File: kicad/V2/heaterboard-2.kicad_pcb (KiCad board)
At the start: 2 copper layers, 12 parts, among them J1 Screw_Terminal_01x02, J2 Conn_01x05_Pin, J3 Conn_01x04_Pin, Q1 Q_NMOS_GDS, U1 LM317_TO-220

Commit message: pcb updates
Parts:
- moved J1 114.5 mm to (50.8, 101.6), turned to 90 degrees
- moved U1 113.6 mm to (50.8, 88.9)
- moved R5 84.2 mm to (48.3, 71.1)
- moved R6 84.2 mm to (48.3, 78.7)
- moved Q1 82.9 mm to (81.3, 78.7)
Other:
- copper layers 2 -> 4
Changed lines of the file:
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@@
   (layers
     (0 "F.Cu" signal)
+    (1 "In1.Cu" signal)
+    (2 "In2.Cu" signal)
     (31 "B.Cu" signal)
     (32 "B.Adhes" user "B.Adhesive")
@@
   )
   (setup
+    (stackup
+      (layer "F.SilkS" (type "Top Silk Screen"))
+      (layer "F.Paste" (type "Top Solder Paste"))
+      (layer "F.Mask" (type "Top Solder Mask") (thickness 0.01))
+      (layer "F.Cu" (type "copper") (thickness 0.035))
+      (layer "dielectric 1" (type "prepreg") (thickness 0.1) (material "FR4") (epsilon_r 4.5) (loss_tangent 0.02))
+      (layer "In1.Cu" (type "copper") (thickness 0.035))
+      (layer "dielectric 2" (type "core") (thickness 1.24) (material "FR4") (epsilon_r 4.5) (loss_tangent 0.02))
+      (layer "In2.Cu" (type "copper") (thickness 0.035))
+      (layer "dielectric 3" (type "prepreg") (thickness 0.1) (material "FR4") (epsilon_r 4.5) (loss_tangent 0.02))
+      (layer "B.Cu" (type "copper") (thickness 0.035))
+      (layer "B.Mask" (type "Bottom Solder Mask") (thickness 0.01))
+      (layer "B.Paste" (type "Bottom Solder Paste"))
+      (layer "B.SilkS" (type "Bottom Silk Screen"))
+      (copper_finish "None")
+      (dielectric_constraints no)
+    )
     (pad_to_mask_clearance 0)
     (pcbplotparams
@@
   (net 37 "Net-(R5--)")
   (footprint "Package_TO_SOT_THT:TO-220-3_Vertical" (layer "F.Cu")
-    (at 162.56 62.62)
+    (at 81.28 78.74)
     (descr "TO-220-3, Vertical, RM 2.54mm, see https://www.vishay.com/docs/66542/to-220-1.pdf")
     (tags "TO-220-3 Vertical RM 2.54mm")
@@
   )
   (footprint "Resistor_THT:R_Axial_DIN0207_L6.3mm_D2.5mm_P10.16mm_Horizontal" (layer "F.Cu")
-    (at 132.08 86.36)
+    (at 48.26 78.74)
     (descr "Resistor, Axial_DIN0207 series, Axial, Horizontal, pin pitch=10.16mm, 0.25W = 1/4W, length*diameter=6.3*2.5mm^2, http://cdn-reichelt.de/documents/datenblatt/B400/1_4W%23YAG.pdf")
     (tags "Resistor Axial_DIN0207 series Axial Horizontal pin pitch 10.16mm 0.25W = 1/4W length 6.3mm diameter 2.5mm")
@@
   )
   (footprint "Package_TO_SOT_THT:TO-220-3_Vertical" (layer "F.Cu")
-    (at 162.56 68.58)
+    (at 50.8 88.9)
     (descr "TO-220-3, Vertical, RM 2.54mm, see https://www.vishay.com/docs/66542/to-220-1.pdf")
     (tags "TO-220-3 Vertical RM 2.54mm")
@@
   )
   (footprint "Resistor_THT:R_Axial_DIN0207_L6.3mm_D2.5mm_P10.16mm_Horizontal" (layer "F.Cu")
-    (at 132.08 78.74)
+    (at 48.26 71.12)
     (descr "Resistor, Axial_DIN0207 series, Axial, Horizontal, pin pitch=10.16mm, 0.25W = 1/4W, length*diameter=6.3*2.5mm^2, http://cdn-reichelt.de/documents/datenblatt/B400/1_4W%23YAG.pdf")
     (tags "Resistor Axial_DIN0207 series Axial Horizontal pin pitch 10.16mm 0.25W = 1/4W length 6.3mm diameter 2.5mm")
@@
   )
   (footprint "Connector_PinHeader_2.54mm:PinHeader_1x02_P2.54mm_Vertical" (layer "F.Cu")
-    (at 161.65 72.94)
+    (at 50.8 101.6 90)
     (descr "Through hole straight pin header, 1x02, 2.54mm pitch, single row")
     (tags "Through hole pin header THT 1x02 2.54mm single row")
@@
     (property "ki_keywords" "screw terminal")
     (attr through_hole)
-    (fp_text reference "J1" (at 0 -2.33) (layer "F.SilkS")
-        (effects (font (size 1 1) (thickness 0.15)))
-    )
-    (fp_text value "Screw_Terminal_01x02" (at 0 4.87) (layer "F.SilkS")
-        (effects (font (size 1 1) (thickness 0.15)))
-    )
-    (fp_text user "${REFERENCE}" (at 0 1.27 90) (layer "F.Fab")
+    (fp_text reference "J1" (at 0 -2.33 90) (layer "F.SilkS")
+        (effects (font (size 1 1) (thickness 0.15)))
+    )
+    (fp_text value "Screw_Terminal_01x02" (at 0 4.87 90) (layer "F.SilkS")
+        (effects (font (size 1 1) (thickness 0.15)))
+    )
+    (fp_text user "${REFERENCE}" (at 0 1.27) (layer "F.Fab")
         (effects (font (size 1 1) (thickness 0.15)))
     )
@@
     (fp_line (start 1.27 3.81) (end -1.27 3.81)
       (stroke (width 0.1) (type solid)) (layer "F.Fab"))
-    (pad "1" thru_hole rect (at 0 0) (size 1.7 1.7) (drill 1) (layers "*.Cu" "*.Mask")
+    (pad "1" thru_hole rect (at 0 0 90) (size 1.7 1.7) (drill 1) (layers "*.Cu" "*.Mask")
       (net 31 "Net-(J1-Pin_1)") (pinfunction "Pin_1") (pintype "passive"))
-    (pad "2" thru_hole oval (at 0 2.54) (size 1.7 1.7) (drill 1) (layers "*.Cu" "*.Mask")
+    (pad "2" thru_hole oval (at 0 2.54 90) (size 1.7 1.7) (drill 1) (layers "*.Cu" "*.Mask")
       (net 32 "+12V") (pinfunction "Pin_2") (pintype "passive"))
     (model "${KICAD6_3DMODEL_DIR}/Connector_PinHeader_2.54mm.3dshapes/PinHeader_1x02_P2.54mm_Vertical.wrl"

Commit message: pcb layout
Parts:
- added C1: 100nF, Capacitor_THT:CP_Radial_D10.0mm_P5.00mm, F.Cu at (127.0, 61.0)
- added C2: 1μF, Capacitor_THT:CP_Radial_D10.0mm_P5.00mm, F.Cu at (142.3, 61.0)
- J1: footprint Connector_PinHeader_2.54mm:PinHeader_1x02_P2.54mm_Vertical -> TerminalBlock:TerminalBlock_Wuerth_691311400102_P7.62mm
- R5: value 0.4 kΩ -> 0.4kΩ
- R6: value 2.4 kΩ -> 2.4kΩ
- moved R6 97.2 mm to (139.7, 45.7)
- moved J1 94.5 mm to (143.5, 83.4), turned to 180 degrees
- moved J2 88.7 mm to (66.0, 81.3), turned to 90 degrees
- moved R5 80.3 mm to (124.5, 45.7)
- moved J3 76.0 mm to (83.8, 81.3), turned to 90 degrees
- moved R1 68.6 mm to (63.5, 45.7)
- moved R2 54.3 mm to (78.7, 45.7)
- moved R3 42.0 mm to (94.0, 45.7)
- moved R4 34.2 mm to (109.2, 45.7)
- moved U1 31.8 mm to (66.0, 61.0)
- moved Q1 17.8 mm to (81.3, 61.0)
- moved A1 7.05 mm to (109.2, 97.8)
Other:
- board outline added: 113.2 x 68.2 mm

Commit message: pcb layout and began routing
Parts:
- added J1: Screw_Terminal_01x02, Connector_Molex:Molex_Mega-Fit_76825-0002_2x01_P5.70mm_Horizontal, F.Cu at (86.4, 87.2)
- J2: renamed from J1; footprint TerminalBlock:TerminalBlock_Wuerth_691311400102_P7.62mm -> Connector_Molex:Molex_Mega-Fit_76825-0002_2x01_P5.70mm_Horizontal
- J3: footprint Connector_PinSocket_2.54mm:PinSocket_1x04_P2.54mm_Vertical -> Connector_Molex:Molex_Micro-Fit_3.0_43650-0400_1x04_P3.00mm_Horizontal
- J4: renamed from J2; footprint Connector_PinHeader_2.54mm:PinHeader_1x05_P2.54mm_Vertical -> Connector_Molex:Molex_Micro-Fit_3.0_43650-0515_1x05_P3.00mm_Vertical
- moved J4 90.7 mm to (154.5, 61.0), turned to 0 degrees
- moved J3 84.1 mm to (166.9, 94.7), turned to 180 degrees
- moved R5 69.4 mm to (157.5, 73.7)
- moved R3 65.3 mm to (127.0, 61.0)
- moved R6 61.5 mm to (157.5, 83.8)
- moved R4 54.5 mm to (127.0, 71.1)
- moved R2 50.1 mm to (96.5, 71.1)
- moved Q1 42.0 mm to (99.1, 99.1)
- moved C1 40.8 mm to (86.4, 64.1), turned to -90 degrees
- moved U1 39.1 mm to (99.1, 81.8)
- moved A1 36.6 mm to (139.7, 118.1)
- moved R1 32.1 mm to (96.5, 61.5)
- moved J2 26.9 mm to (116.8, 86.8)
- moved C2 25.7 mm to (116.8, 64.1), turned to -90 degrees
- renumbered R5 to R1, R6 to R2, R1 to R3, R2 to R4, R3 to R5, R4 to R6
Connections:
- R4 pad 2: unconnected-(R2---Pad2) -> GND
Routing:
- net +9V: track 0.00 -> 98.1 mm
- net /A0: track 0.00 -> 17.3 mm
- net /A1: track 0.00 -> 17.3 mm
- net Net-(R1--): track 0.00 -> 16.8 mm
- net GND: track 0.00 -> 11.0 mm
- added copper zone on In1.Cu, net (none)
- added copper zone on In2.Cu, net (none)
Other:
- outline, holes or cut-outs redrawn

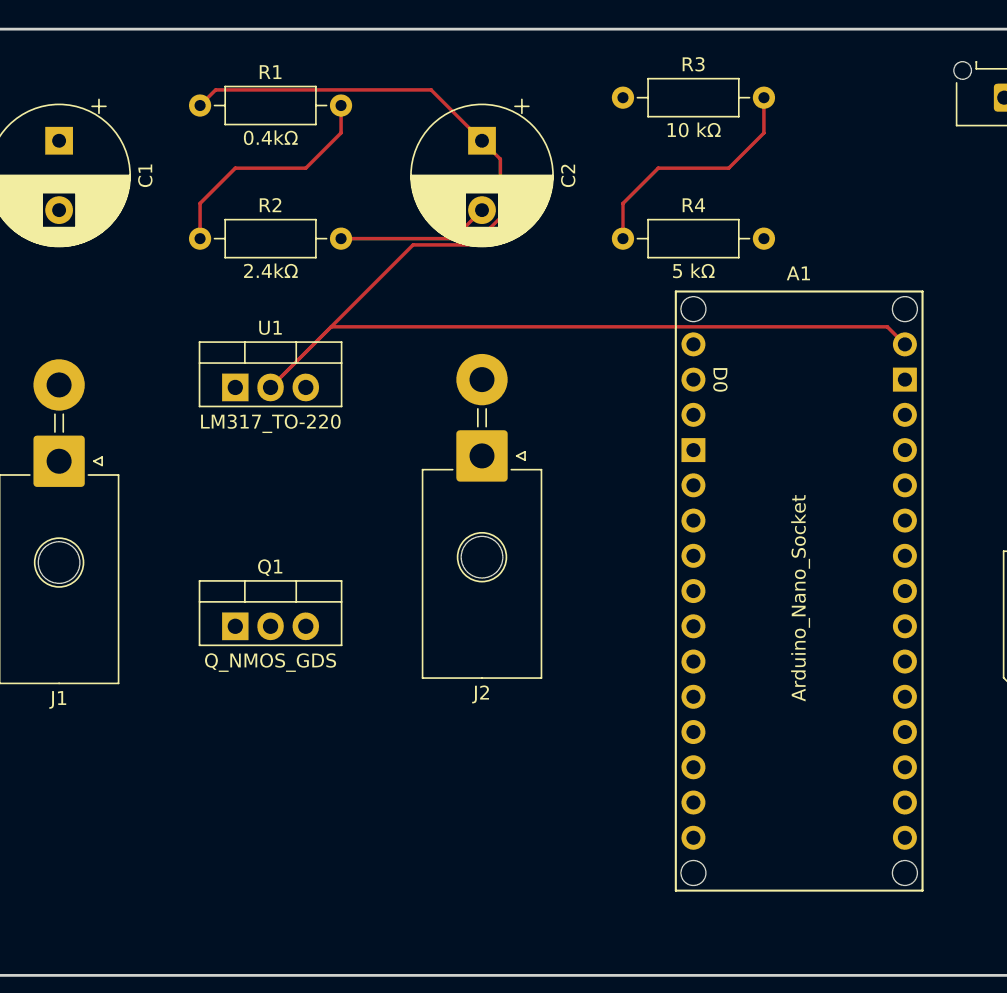
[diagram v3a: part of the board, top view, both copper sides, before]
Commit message: updated layout
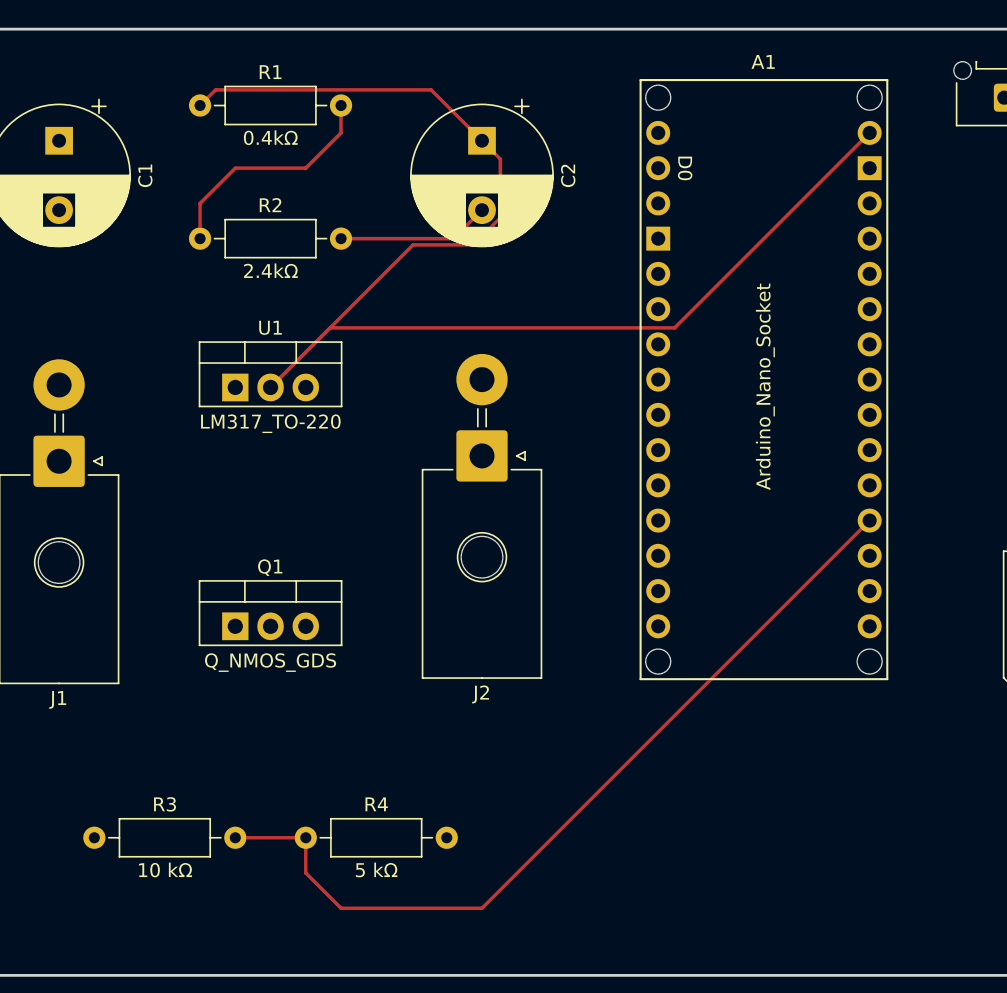
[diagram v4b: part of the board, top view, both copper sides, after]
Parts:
- J1: value Screw_Terminal_01x02 -> PWR IN
- J2: value Screw_Terminal_01x02 -> HEATER
- moved R3 65.5 mm to (88.9, 114.3)
- moved R4 48.9 mm to (104.1, 114.3)
- moved A1 15.5 mm to (137.2, 102.9)
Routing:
- net /A0: track 17.3 -> 60.9 mm
- net +9V: track 98.1 -> 100.8 mm
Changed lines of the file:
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@@
         (effects (font (size 1 1) (thickness 0.15)))
     )
-    (fp_text value "Screw_Terminal_01x02" (at 0 8.55) (layer "F.Fab")
+    (fp_text value "PWR IN" (at 0 8.55) (layer "F.Fab")
         (effects (font (size 1 1) (thickness 0.15)))
     )
@@
   )
   (footprint "PCM_arduino-library:Arduino_Nano_Socket" (layer "F.Cu")
-    (at 139.7 118.11)
+    (at 137.16 102.87)
     (descr "https://docs.arduino.cc/hardware/nano")
     (property "Sheetfile" "heaterboard-2.kicad_sch")
@@
   )
   (footprint "Resistor_THT:R_Axial_DIN0207_L6.3mm_D2.5mm_P10.16mm_Horizontal" (layer "F.Cu")
-    (at 127 71.12)
+    (at 104.14 114.3)
     (descr "Resistor, Axial_DIN0207 series, Axial, Horizontal, pin pitch=10.16mm, 0.25W = 1/4W, length*diameter=6.3*2.5mm^2, http://cdn-reichelt.de/documents/datenblatt/B400/1_4W%23YAG.pdf")
     (tags "Resistor Axial_DIN0207 series Axial Horizontal pin pitch 10.16mm 0.25W = 1/4W length 6.3mm diameter 2.5mm")
@@
   )
   (footprint "Resistor_THT:R_Axial_DIN0207_L6.3mm_D2.5mm_P10.16mm_Horizontal" (layer "F.Cu")
-    (at 127 60.96)
+    (at 88.9 114.3)
     (descr "Resistor, Axial_DIN0207 series, Axial, Horizontal, pin pitch=10.16mm, 0.25W = 1/4W, length*diameter=6.3*2.5mm^2, http://cdn-reichelt.de/documents/datenblatt/B400/1_4W%23YAG.pdf")
     (tags "Resistor Axial_DIN0207 series Axial Horizontal pin pitch 10.16mm 0.25W = 1/4W length 6.3mm diameter 2.5mm")
@@
         (effects (font (size 1 1) (thickness 0.15)))
     )
-    (fp_text value "Screw_Terminal_01x02" (at 0 8.55 180) (layer "F.Fab")
+    (fp_text value "HEATER" (at 0 8.55 180) (layer "F.Fab")
         (effects (font (size 1 1) (thickness 0.15)))
     )
@@
   (gr_line (start 176.72 72.12) (end 180.82 72.12)
     (stroke (width 0.2) (type solid)) (layer "Edge.Cuts"))
-  (segment (start 129.54 66.04) (end 134.62 66.04) (width 0.25) (layer "F.Cu") (net 3))
-  (segment (start 127 71.12) (end 127 68.58) (width 0.25) (layer "F.Cu") (net 3))
-  (segment (start 134.62 66.04) (end 137.16 63.5) (width 0.25) (layer "F.Cu") (net 3))
-  (segment (start 127 68.58) (end 129.54 66.04) (width 0.25) (layer "F.Cu") (net 3))
-  (segment (start 137.16 63.5) (end 137.16 60.96) (width 0.25) (layer "F.Cu") (net 3))
+  (segment (start 104.14 116.84) (end 106.68 119.38) (width 0.25) (layer "F.Cu") (net 3))
+  (segment (start 99.06 114.3) (end 104.14 114.3) (width 0.25) (layer "F.Cu") (net 3))
+  (segment (start 116.84 119.38) (end 144.78 91.44) (width 0.25) (layer "F.Cu") (net 3))
+  (segment (start 104.14 114.3) (end 104.14 116.84) (width 0.25) (layer "F.Cu") (net 3))
+  (segment (start 106.68 119.38) (end 116.84 119.38) (width 0.25) (layer "F.Cu") (net 3))
   (segment (start 157.48 83.82) (end 157.48 81.28) (width 0.25) (layer "F.Cu") (net 4))
   (segment (start 165.1 78.74) (end 167.64 76.2) (width 0.25) (layer "F.Cu") (net 4))
@@
   (segment (start 114.785 71.12) (end 106.68 71.12) (width 0.25) (layer "F.Cu") (net 27))
   (segment (start 116.84 69.065) (end 114.785 71.12) (width 0.25) (layer "F.Cu") (net 27))
-  (segment (start 146.055 77.475) (end 105.97 77.475) (width 0.25) (layer "F.Cu") (net 30))
   (segment (start 116.84 64.065) (end 113.175 60.4) (width 0.25) (layer "F.Cu") (net 30))
   (segment (start 111.875 71.57) (end 116.208833 71.57) (width 0.25) (layer "F.Cu") (net 30))
   (segment (start 118.165 65.39) (end 116.84 64.065) (width 0.25) (layer "F.Cu") (net 30))
   (segment (start 113.175 60.4) (end 97.645 60.4) (width 0.25) (layer "F.Cu") (net 30))
+  (segment (start 105.8936 77.5514) (end 130.7286 77.5514) (width 0.25) (layer "F.Cu") (net 30))
   (segment (start 97.645 60.4) (end 96.52 61.525) (width 0.25) (layer "F.Cu") (net 30))
   (segment (start 116.208833 71.57) (end 118.165 69.613833) (width 0.25) (layer "F.Cu") (net 30))
   (segment (start 101.6 81.845) (end 111.875 71.57) (width 0.25) (layer "F.Cu") (net 30))
   (segment (start 118.165 69.613833) (end 118.165 65.39) (width 0.25) (layer "F.Cu") (net 30))
-  (segment (start 147.32 78.74) (end 146.055 77.475) (width 0.25) (layer "F.Cu") (net 30))
-  (segment (start 105.97 77.475) (end 101.6 81.845) (width 0.25) (layer "F.Cu") (net 30))
+  (segment (start 101.6 81.845) (end 105.8936 77.5514) (width 0.25) (layer "F.Cu") (net 30))
+  (segment (start 130.7286 77.5514) (end 144.78 63.5) (width 0.25) (layer "F.Cu") (net 30))
   (segment (start 96.52 71.12) (end 96.52 68.58) (width 0.25) (layer "F.Cu") (net 35))
   (segment (start 96.52 68.58) (end 99.06 66.04) (width 0.25) (layer "F.Cu") (net 35))
@@
         (xy 78.74 109.14)
         (xy 124.46 109.14)
-        (xy 124.46 58.34)
-        (xy 78.74 58.34)
+        (xy 124.46 76.12)
+        (xy 78.74 76.12)
       )
     )
@@
       (pts
         (xy 78.74 66.04)
-        (xy 78.74 66.04)
         (xy 78.74 58.42)
         (xy 172.72 58.42)
@@
         (xy 78.74 121.92)
         (xy 78.74 83.82)
-        (xy 78.74 83.82)
       )

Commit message: end of class 15 feb
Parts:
- C1, C2: footprint Capacitor_THT:CP_Radial_D10.0mm_P5.00mm -> Capacitor_SMD:C_1206_3216Metric_Pad1.33x1.80mm_HandSolder
- J1: value PWR IN -> Screw_Terminal_01x02
- J2: value HEATER -> Screw_Terminal_01x02
- R1, R2, R3, R4, R5, R6: footprint Resistor_THT:R_Axial_DIN0207_L6.3mm_D2.5mm_P10.16mm_Horizontal -> Resistor_SMD:R_1206_3216Metric_Pad1.30x1.75mm_HandSolder
- moved R3 78.6 mm to (153.0, 68.9), turned to 90 degrees
- moved R4 69.5 mm to (156.8, 68.9), turned to 90 degrees
- moved C1 21.5 mm to (105.4, 74.0), turned to 90 degrees
- moved J4 20.3 mm to (154.9, 81.3)
- moved C2 18.2 mm to (101.6, 74.0), turned to 90 degrees
- moved R6 16.4 mm to (164.5, 68.9), turned to 90 degrees
- moved R1 12.7 mm to (94.0, 73.9), turned to 90 degrees
- moved R5 5.69 mm to (160.7, 68.9), turned to 90 degrees
- moved R2 3.16 mm to (97.8, 74.0), turned to 90 degrees
- moved J3 2.35 mm to (164.5, 94.7)
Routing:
- net /D9: track 0.00 -> 33.6 mm
- net /A0: track 60.9 -> 31.0 mm
- net /A1: track 17.3 -> 44.5 mm
- net +9V: track 100.8 -> 75.6 mm
- net /A5: track 0.00 -> 21.7 mm
- net /A4: track 0.00 -> 17.9 mm
- net Net-(J4-Pin_3): track 0.00 -> 10.9 mm
- net Net-(U1-ADJ): track 16.8 -> 11.9 mm
- net +12V: track 0.00 -> 3.86 mm, vias 0 -> 2
- net GND: track 11.0 -> 9.75 mm, vias 0 -> 5
- added copper zone on In2.Cu, net +12V
- added copper zone on In1.Cu, net GND
- added copper zone on In2.Cu, net Net-(J2-Pin_1)
- removed copper zone on In1.Cu, net (none)
- removed copper zone on In2.Cu, net (none)
